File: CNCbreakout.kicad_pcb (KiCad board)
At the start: 2 copper layers, 126 parts, among them P101 X1, P102 X2, P103 Y, P104 Z, P105 GND, P106 +24V, P107 VFD_Stop, P108 VFD_FwdRev, P109 VFD_Aux, P110 Z_STOP, P111 XY_STOP, P112 VFD_IN, P113 Zaux1, P114 Zaux2, P115 Zaux3, P116 VFD_Speed, P117 VFD_Temp, P118 Enable, Q301 Q_NPN_CBE, Q302 Q_NPN_CBE, Q303 Q_NPN_CBE, Q304 Q_NPN_CBE, Q305 Q_NPN_CBE, Q306 Q_NPN_CBE, Q307 Q_NPN_CBE, Q308 Q_NPN_CBE, Q309 Q_NPN_CBE, Q310 Q_NPN_CBE, Q311 Q_NPN_CBE, Q312 Q_NPN_CBE, Q313 Q_NPN_CBE, Q314 Q_NPN_CBE, Q315 Q_NPN_CBE, Q316 Q_NPN_CBE, Q317 Q_NPN_CBE, Q318 Q_NPN_CBE, U301 TCMT1108, U302 TCMT1108, U601 TCMT1108, U602 TCMT1108, U603 TCMT1108, U604 TCMT1108

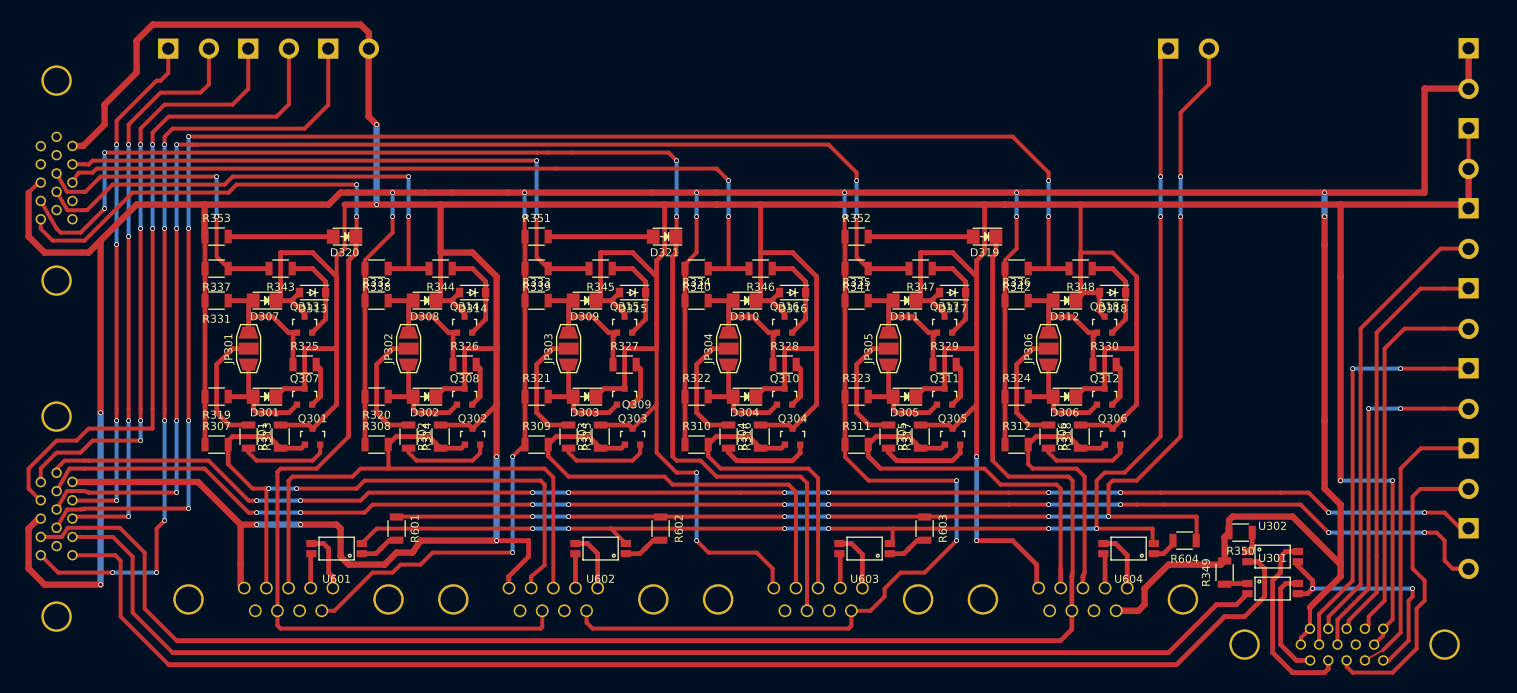
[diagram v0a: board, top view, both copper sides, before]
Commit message: checked limits and homes, removed enable, adjusted routing
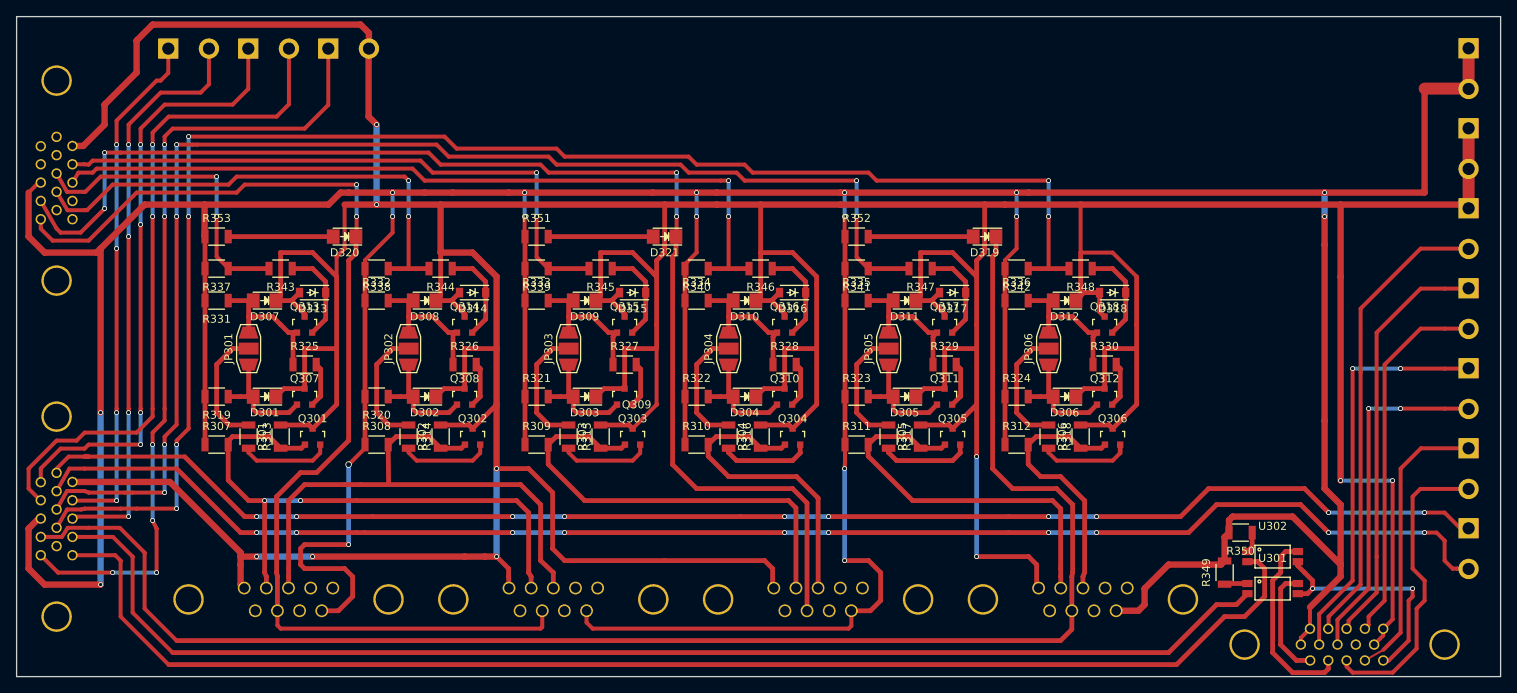
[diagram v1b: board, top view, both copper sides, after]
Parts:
- removed P118: Enable, Connect:bornier2
- removed R601, R602, R603, R604: R, Resistors_SMD:R_1206
- removed U601, U602, U603, U604: TCMT1108, CNCbreakout:TCMT1108
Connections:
- P101 pad 4: /Estop_Logic/X1EN+ -> (no net)
- P101 pad 5: /Estop_Logic/X1EN- -> (no net)
- P101 pad 6: Net-(P101-Pad6) -> (no net)
- P101 pad 8: Net-(P101-Pad8) -> (no net)
- P102 pad 4: /Estop_Logic/X2EN+ -> (no net)
- P102 pad 5: /Estop_Logic/X2EN- -> (no net)
- P102 pad 6: Net-(P102-Pad6) -> (no net)
- P102 pad 8: Net-(P102-Pad8) -> (no net)
- P103 pad 4: /Estop_Logic/YEN+ -> (no net)
- P103 pad 5: /Estop_Logic/YEN- -> (no net)
- P103 pad 6: Net-(P103-Pad6) -> (no net)
- P103 pad 8: Net-(P103-Pad8) -> (no net)
- P104 pad 4: /Estop_Logic/ZEN+ -> (no net)
- P104 pad 5: /Estop_Logic/ZEN- -> (no net)
- P104 pad 6: Net-(P104-Pad6) -> (no net)
- P104 pad 8: Net-(P104-Pad8) -> (no net)
- P110 pad 10: ShieldZ -> (no net)
- P111 pad 10: ShieldXY -> (no net)
- P111 pad 11: Net-(P111-Pad11) -> (no net)
- P111 pad 12: Net-(P111-Pad12) -> (no net)
- P111 pad 4: Net-(P111-Pad4) -> (no net)
- P111 pad 5: Net-(P111-Pad5) -> (no net)
- P111 pad 6: Net-(P111-Pad6) -> (no net)
- P111 pad 7: Net-(P111-Pad7) -> (no net)
- P112 pad 9: Net-(P112-Pad9) -> (no net)
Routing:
- net /Estop_Logic/ENABLE-: track 171.6 -> 0.00 mm, vias 8 -> 0
- net /Estop_Logic/ENABLE+: track 168.6 -> 0.00 mm, vias 8 -> 0
- net +24V: track 677.8 -> 657.3 mm
- net /Estop_Logic/ZEN-: track 7.69 -> 0.00 mm
- net /Estop_Logic/YEN-: track 7.65 -> 0.00 mm
- net /Estop_Logic/X2EN-: track 7.60 -> 0.00 mm
- net /Estop_Logic/X1EN-: track 7.56 -> 0.00 mm
- net F1_LIM: track 81.1 -> 75.2 mm
- net Net-(R603-Pad2): track 5.12 -> 0.00 mm
- net Net-(R602-Pad2): track 5.08 -> 0.00 mm
- net Net-(R601-Pad2): track 5.08 -> 0.00 mm
- net /Estop_Logic/ZEN+: track 4.38 -> 0.00 mm
- net /Estop_Logic/YEN+: track 4.34 -> 0.00 mm
- net /Estop_Logic/X1EN+: track 4.33 -> 0.00 mm
- net /Estop_Logic/X2EN+: track 4.30 -> 0.00 mm
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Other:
- board outline added: 185.5 x 82.5 mm
